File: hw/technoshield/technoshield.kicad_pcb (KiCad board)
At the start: 2 copper layers, 68.6 x 53.3 mm, 9 parts, among them P1 Power, P2 Analog, P3 Digital, P4 Digital, P5 CONN_1, P6 CONN_1, P7 CONN_1, P8 CONN_1

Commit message: During dev PCB.
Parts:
- removed DS2: LCD16X2, Displays:WC1602A
- removed P6, P7, P8: CONN_1, Socket_Arduino_Uno:Arduino_1pin
- added C1: 0.1uF, Capacitors_THT:C_Disc_D3.0mm_W1.6mm_P2.50mm, F.Cu at (128.8, 107.6)
- added C2: 0.1uF, Capacitors_THT:C_Disc_D3.0mm_W1.6mm_P2.50mm, F.Cu at (118.6, 108.0)
- added C3: 0.1uF, Capacitors_THT:C_Disc_D3.0mm_W1.6mm_P2.50mm, F.Cu at (162.8, 84.6)
- added C4: 0.1uF, Capacitors_THT:C_Disc_D3.0mm_W1.6mm_P2.50mm, F.Cu at (149.7, 87.1)
- added C5: 0.1uF, Capacitors_THT:C_Disc_D3.0mm_W1.6mm_P2.50mm, F.Cu at (157.2, 34.2)
- added C6: 0.1uF, Capacitors_THT:C_Disc_D3.0mm_W1.6mm_P2.50mm, F.Cu at (131.8, 125.5)
- added D1: LS T67K-J1K2-1-Z, T67K:T67K, F.Cu at (181.4, 73.5)
- added D2: LY T67K-J2L1-26-Z, T67K:T67K, F.Cu at (185.7, 73.5)
- added D3: LP T67K-E1F2-25-Z, T67K:T67K, F.Cu at (190.0, 73.5)
- added D4: LP T67K-E1F2-25-Z, T67K:T67K, F.Cu at (112.8, 107.4)
- added DS1: LCD-016N002L, Displays:WC1602A, F.Cu at (121.7, 38.0)
- added J1: 101-00303-68-1-ND, Connectors_lib:MICRO_SD_HINGE_AMP, F.Cu at (124.5, 117.0)
- added JP1: JUMPER, Pin_Headers:Pin_Header_Straight_1x02_Pitch2.54mm, F.Cu at (188.1, 130.6)
- added JP2: JUMPER, Pin_Headers:Pin_Header_Straight_1x02_Pitch2.54mm, F.Cu at (181.0, 130.6)
- added JP3: JUMPER, Pin_Headers:Pin_Header_Straight_1x02_Pitch2.54mm, F.Cu at (191.4, 130.6)
- added JP4: JUMPER, Pin_Headers:Pin_Header_Straight_1x02_Pitch2.54mm, F.Cu at (184.3, 130.6)
- added JP5: JUMPER, Pin_Headers:Pin_Header_Straight_1x02_Pitch2.54mm, F.Cu at (173.7, 130.6)
- added JP6: JUMPER, Pin_Headers:Pin_Header_Straight_1x02_Pitch2.54mm, F.Cu at (177.0, 130.6)
- added Q1: MMBT2222A-7-F, TO_SOT_Packages_SMD:SOT-23, F.Cu at (114.0, 86.7)
- added R1: 10k, Resistors_THT:R_Axial_DIN0204_L3.6mm_D1.6mm_P7.62mm_Horizontal, F.Cu at (142.7, 100.2)
- added R11: 1.6k, Resistors_THT:R_Axial_DIN0204_L3.6mm_D1.6mm_P7.62mm_Horizontal, F.Cu at (176.5, 92.1)
- added R12: 1.6k, Resistors_THT:R_Axial_DIN0204_L3.6mm_D1.6mm_P7.62mm_Horizontal, F.Cu at (176.5, 94.5)
- added R13: 1.6k, Resistors_THT:R_Axial_DIN0204_L3.6mm_D1.6mm_P7.62mm_Horizontal, F.Cu at (176.5, 96.9)
- added R14: 4k7, Resistors_THT:R_Axial_DIN0204_L3.6mm_D1.6mm_P7.62mm_Horizontal, F.Cu at (168.9, 101.7)
- added R15: 4k7, Resistors_THT:R_Axial_DIN0204_L3.6mm_D1.6mm_P7.62mm_Horizontal, F.Cu at (168.9, 99.3)
- added R16: 750, Resistors_THT:R_Axial_DIN0204_L3.6mm_D1.6mm_P7.62mm_Horizontal, F.Cu at (115.3, 100.1)
- added R2: 10k, Resistors_THT:R_Axial_DIN0204_L3.6mm_D1.6mm_P7.62mm_Horizontal, F.Cu at (138.2, 100.2)
- added R3: 10k, Resistors_THT:R_Axial_DIN0204_L3.6mm_D1.6mm_P7.62mm_Horizontal, F.Cu at (145.0, 100.2)
- added R4: 10k, Resistors_THT:R_Axial_DIN0204_L3.6mm_D1.6mm_P7.62mm_Horizontal, F.Cu at (140.5, 100.2)
- added R7: 10k, Resistors_THT:R_Axial_DIN0204_L3.6mm_D1.6mm_P7.62mm_Horizontal, F.Cu at (112.9, 92.5)
- added REF***: OSHW-Symbol_13.4x12mm_SilkScreen, Symbols:OSHW-Symbol_13.4x12mm_SilkScreen, B.Cu at (152.1, 54.2)
- added RV1: 10k, POTENTIOMETRES:POTENTIOMETRE_BOURNS_3319P, F.Cu at (123.1, 77.2)
- added SW1: SW_PUSH, smt_btn:smt_btn, F.Cu at (183.6, 85.2)
- added SW2: SW_PUSH, smt_btn:smt_btn, F.Cu at (185.9, 98.7)
- added SW3: SW_PUSH, smt_btn:smt_btn, F.Cu at (194.6, 98.7)
- added SW4: SW_PUSH, smt_btn:smt_btn, F.Cu at (183.6, 107.1)
- added SW5: SW_PUSH, smt_btn:smt_btn, F.Cu at (183.6, 117.2)
- added SW6: SW_PUSH, smt_btn:smt_btn, F.Cu at (155.7, 131.4)
- added U1: PDM1-S5-D15-S, PDM1-S:PDM1-S, F.Cu at (124.5, 131.8)
- added U2: MCP23008, Housings_DIP:DIP-18_W7.62mm_LongPads, F.Cu at (155.1, 87.5)
- added U3: MCP23008, Housings_DIP:DIP-18_W7.62mm_LongPads, F.Cu at (128.8, 104.6)
- added U4: HEF4050B, SO16-3_9mm:SO16-3_9mm, F.Cu at (138.4, 93.9)
- P1: value Power -> CONN_01X03; footprint Socket_Arduino_Uno:Socket_Strip_Arduino_1x08 -> Pin_Headers:Pin_Header_Straight_1x03_Pitch2.54mm
- P2: value Analog -> Power; footprint Socket_Arduino_Uno:Socket_Strip_Arduino_1x06 -> Socket_Arduino_Uno:Socket_Strip_Arduino_1x08
- P3: value Digital -> Analog; footprint Socket_Arduino_Uno:Socket_Strip_Arduino_1x10 -> Socket_Arduino_Uno:Socket_Strip_Arduino_1x06
- P4: footprint Socket_Arduino_Uno:Socket_Strip_Arduino_1x08 -> Socket_Arduino_Uno:Socket_Strip_Arduino_1x10
- P5: value CONN_1 -> Digital; footprint Socket_Arduino_Uno:Arduino_1pin -> Socket_Arduino_Uno:Socket_Strip_Arduino_1x08
- moved P3 57.9 mm to (161.8, 123.8)
- moved P5 57.8 mm to (156.7, 75.6)
- moved P4 26.9 mm to (129.8, 75.6)
- moved P2 22.9 mm to (138.9, 123.8)
- moved P1 8.52 mm to (141.5, 132.0), turned to 90 degrees
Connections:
- P1 pad 2: /IOREF -> Net-(P1-Pad2)
- P1 pad 3: /Reset -> Net-(P1-Pad3)
- P2 pad 1: /A0 -> Net-(P2-Pad1)
- P2 pad 2: /A1 -> /IOREF
- P2 pad 3: /A2 -> /Reset
- P2 pad 4: /A3 -> +3V3
- P2 pad 5: /A4(SDA) -> +5V
- P2 pad 6: /A5(SCL) -> GND
- P3 pad 1: /A5(SCL) -> /A0
- P3 pad 2: /A4(SDA) -> /A1
- P3 pad 3: /AREF -> /A2
- P3 pad 4: GND -> /A3
- P3 pad 5: /13(SCK) -> /A4(SDA)
- P3 pad 6: /12(MISO) -> /A5(SCL)
- P4 pad 1: /7 -> /A5(SCL)
- P4 pad 2: /6(**) -> /A4(SDA)
- P4 pad 3: /5(**) -> /AREF
- P4 pad 4: /4 -> GND
- P4 pad 5: /3(**) -> /13(SCK)
- P4 pad 6: /2 -> /12(MISO)
- P4 pad 7: /1(Tx) -> /11(**/MOSI)
- P4 pad 8: /0(Rx) -> /10(**/SS)
- P5 pad 1: Net-(P5-Pad1) -> /7
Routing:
- net /A5(SCL): track 0.00 -> 177.1 mm, vias 0 -> 2
- net /A4(SDA): track 0.00 -> 130.1 mm
- net +3V3: track 0.00 -> 96.3 mm
- net Net-(DS1-Pad14): track 0.00 -> 76.7 mm
- net Net-(DS1-Pad13): track 0.00 -> 74.4 mm
- net Net-(DS1-Pad11): track 0.00 -> 72.7 mm, vias 0 -> 1
- net Net-(DS1-Pad12): track 0.00 -> 71.0 mm
- net Net-(DS1-Pad6): track 0.00 -> 60.9 mm, vias 0 -> 1
- net Net-(D4-Pad1): track 0.00 -> 57.5 mm, vias 0 -> 2
- net Net-(J1-Pad3): track 0.00 -> 55.4 mm, vias 0 -> 2
- net Net-(DS1-Pad4): track 0.00 -> 53.9 mm
- net Net-(J1-Pad5): track 0.00 -> 53.4 mm, vias 0 -> 4
- net Net-(SW3-Pad1): track 0.00 -> 47.0 mm, vias 0 -> 2
- net Net-(R16-Pad2): track 0.00 -> 44.5 mm, vias 0 -> 1
- net Net-(DS1-Pad3): track 0.00 -> 40.8 mm
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- added copper zone on F.Cu, net +5V
- added copper zone on B.Cu, net GND
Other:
- board size 68.6 x 53.3 mm -> 85.9 x 102.1 mm
- board text added: "+"
- board text added: "-"
- board text added: "0"
- board text added: "12"
- board text added: "13"
- board text added: "2"
- board text added: "3.3V"
- board text added: "4"
- board text added: "5V"
- board text added: "7"
- board text added: "8"
- board text added: "A0"
- board text added: "A1"
- board text added: "A2"
- board text added: "A3"
- board text added: "A4"
- board text added: "A5"
- board text added: "AREF"
- board text added: "But/LED"
- board text added: "GND"
- board text added: "I2C Addr"
- board text added: "I2C Pull-up"
- board text added: "IOREF"
- board text added: "LCD"
- board text added: "PWR +/-15V"
- board text added: "RESET"
- board text added: "RX<-0"
- board text added: "Reset"
- board text added: "SCL"
- board text added: "SDA"
- board text added: "TX->1"
- board text added: "Technoshield - User Interface Dépertement de Génie Physique Cégep La Poactière"
- board text added: "VIN"
- board text added: "_________________"
- board text added: "| Board | Rev: --"
- board text added: "| Technoshield - User Interface | Génie Physique, Cégep La Pocatière"
- board text added: "| |"
- board text added: "~~10"
- board text added: "~~11"
- board text added: "~~3"
- board text added: "~~5"
- board text added: "~~6"
- board text added: "~~9"
- board text removed: "1"

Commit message: Dev of Rev -- almost finish.
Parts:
- moved P1 2.54 mm to (144.0, 132.0), turned to 270 degrees
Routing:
- net Net-(DS1-Pad16): track 0.00 -> 71.1 mm, vias 0 -> 1
- net GND: track 0.00 -> 64.2 mm, vias 0 -> 24
- net Net-(JP4-Pad2): track 16.5 -> 76.6 mm, vias 0 -> 1
- net /12(MISO): track 0.00 -> 59.6 mm, vias 0 -> 2
- net Net-(JP3-Pad2): track 11.2 -> 69.2 mm
- net Net-(JP2-Pad2): track 12.1 -> 69.2 mm
- net Net-(JP1-Pad2): track 14.4 -> 71.3 mm, vias 0 -> 1
- net +5V: track 11.8 -> 55.4 mm, vias 0 -> 2
- net Net-(JP5-Pad1): track 0.00 -> 38.7 mm, vias 0 -> 2
- net /A5(SCL): track 177.1 -> 138.9 mm, vias 2 -> 1
- net Net-(JP6-Pad1): track 0.00 -> 33.4 mm, vias 0 -> 1
- net Net-(D3-Pad2): track 0.00 -> 29.9 mm, vias 0 -> 1
- net Net-(P1-Pad1): track 0.00 -> 27.4 mm
- net Net-(D2-Pad2): track 0.00 -> 23.9 mm, vias 0 -> 1
- net /Reset: track 0.00 -> 23.4 mm
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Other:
- board text added: "Board Rev: --"
- board text added: "Technoshield - User Interface Génie Physique, Cégep La Pocatière"
- board text removed: "| Board | Rev: --"
- board text removed: "| Technoshield - User Interface | Génie Physique, Cégep La Pocatière"

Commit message: Gerber done.
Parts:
- moved C5 38.2 mm to (195.3, 37.2), turned to 270 degrees
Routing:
- net +5V: track 55.4 -> 96.8 mm
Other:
- board size 85.9 x 102.1 mm -> 85.9 x 99.9 mm
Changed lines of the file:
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@@
     (links 126)
     (no_connects 0)
-    (area 104.337905 32.309999 209.860096 138.997)
+    (area 110.922999 34.468999 196.925001 134.568001)
     (thickness 1.6)
-    (drawings 55)
-    (tracks 455)
+    (drawings 56)
+    (tracks 460)
     (zones 0)
     (modules 47)
@@
     (rev --)
     (company "Cégep La Pocatiere")
-    (comment 1 https://creativecommons.org/licenses/by-sa/4.0/)
-    (comment 2 "Released under the Creative Commons Attribution Share-Alike 4.0 License")
-    (comment 3 "Jean-Sébastien Castonguay")
+    (comment 1 "Adapted from https://learn.adafruit.com/i2c-spi-lcd-backpack")
+    (comment 2 https://creativecommons.org/licenses/by-sa/4.0/)
+    (comment 3 "Released under the Creative Commons Attribution Share-Alike 4.0 License")
+    (comment 4 "Copyright 2017 Jean-Sébastien Castonguay")
   )
   (layers
@@
     (pad_drill 1.016)
     (pad_to_mask_clearance 0)
+    (pad_to_paste_clearance -0.127)
     (aux_axis_origin 110.998 126.365)
     (grid_origin 176.53 82.042)
     (visible_elements 7FFFFFFF)
     (pcbplotparams
-      (layerselection 0x00030_80000001)
+      (layerselection 0x010fc_80000001)
       (usegerberextensions false)
       (excludeedgelayer true)
@@
       (drillshape 0)
       (scaleselection 1)
-      (outputdirectory ""))
+      (outputdirectory gerber/))
   )
   (net 0 "")
@@
   )
   (module Capacitors_THT:C_Disc_D3.0mm_W1.6mm_P2.50mm (layer F.Cu)
-    (at 157.226 34.163 180)
+    (at 195.326 37.211 270)
     (descr "C, Disc series, Radial, pin pitch=2.50mm, , diameter*width=3.0*1.6mm^2, Capacitor, http://www.vishay.com/docs/45233/krseries.pdf")
     (tags "C Disc series Radial pin pitch 2.50mm  diameter 3.0mm width 1.6mm Capacitor")
-    (fp_text reference C5 (at 4.699 0.127 180) (layer F.SilkS)
-      (effects (font (size 1 1) (thickness 0.15)))
-    )
-    (fp_text value 0.1uF (at -3.175 0 180) (layer F.SilkS)
+    (fp_text reference C5 (at 4.699 0.127 270) (layer F.SilkS)
+      (effects (font (size 1 1) (thickness 0.15)))
+    )
+    (fp_text value 0.1uF (at 8.128 0.127 270) (layer F.SilkS)
+      (effects (font (size 1 1) (thickness 0.15)))
+    )
+    (fp_line (start -0.25 -0.8) (end -0.25 0.8) (layer F.Fab) (width 0.1))
+    (fp_line (start -0.25 0.8) (end 2.75 0.8) (layer F.Fab) (width 0.1))
+    (fp_line (start 2.75 0.8) (end 2.75 -0.8) (layer F.Fab) (width 0.1))
+    (fp_line (start 2.75 -0.8) (end -0.25 -0.8) (layer F.Fab) (width 0.1))
+    (fp_line (start 0.663 -0.861) (end 1.837 -0.861) (layer F.SilkS) (width 0.12))
+    (fp_line (start 0.663 0.861) (end 1.837 0.861) (layer F.SilkS) (width 0.12))
+    (fp_line (start -1.05 -1.15) (end -1.05 1.15) (layer F.CrtYd) (width 0.05))
+    (fp_line (start -1.05 1.15) (end 3.55 1.15) (layer F.CrtYd) (width 0.05))
+    (fp_line (start 3.55 1.15) (end 3.55 -1.15) (layer F.CrtYd) (width 0.05))
+    (fp_line (start 3.55 -1.15) (end -1.05 -1.15) (layer F.CrtYd) (width 0.05))
+    (pad 1 thru_hole circle (at 0 0 270) (size 1.6 1.6) (drill 0.8) (layers *.Cu *.Mask)
+      (net 3 +5V))
+    (pad 2 thru_hole circle (at 2.5 0 270) (size 1.6 1.6) (drill 0.8) (layers *.Cu *.Mask)
+      (net 4 GND))
+    (model Capacitors_ThroughHole.3dshapes/C_Disc_D3.0mm_W1.6mm_P2.50mm.wrl
+      (at (xyz 0 0 0))
+      (scale (xyz 0.393701 0.393701 0.393701))
+      (rotate (xyz 0 0 0))
+    )
+  )
+  (module Capacitors_THT:C_Disc_D3.0mm_W1.6mm_P2.50mm (layer F.Cu)
+    (at 131.826 125.476 180)
+    (descr "C, Disc series, Radial, pin pitch=2.50mm, , diameter*width=3.0*1.6mm^2, Capacitor, http://www.vishay.com/docs/45233/krseries.pdf")
+    (tags "C Disc series Radial pin pitch 2.50mm  diameter 3.0mm width 1.6mm Capacitor")
+    (fp_text reference C6 (at -2.159 0.127 180) (layer F.SilkS)
+      (effects (font (size 1 1) (thickness 0.15)))
+    )
+    (fp_text value 0.1uF (at 1.25 1.86 180) (layer F.SilkS)
       (effects (font (size 1 1) (thickness 0.15)))
     )
@@
     )
   )
-  (module Capacitors_THT:C_Disc_D3.0mm_W1.6mm_P2.50mm (layer F.Cu)
-    (at 131.826 125.476 180)
-    (descr "C, Disc series, Radial, pin pitch=2.50mm, , diameter*width=3.0*1.6mm^2, Capacitor, http://www.vishay.com/docs/45233/krseries.pdf")
-    (tags "C Disc series Radial pin pitch 2.50mm  diameter 3.0mm width 1.6mm Capacitor")
-    (fp_text reference C6 (at -2.159 0.127 180) (layer F.SilkS)
-      (effects (font (size 1 1) (thickness 0.15)))
-    )
-    (fp_text value 0.1uF (at 1.25 1.86 180) (layer F.SilkS)
-      (effects (font (size 1 1) (thickness 0.15)))
-    )
-    (fp_line (start -0.25 -0.8) (end -0.25 0.8) (layer F.Fab) (width 0.1))
-    (fp_line (start -0.25 0.8) (end 2.75 0.8) (layer F.Fab) (width 0.1))
-    (fp_line (start 2.75 0.8) (end 2.75 -0.8) (layer F.Fab) (width 0.1))
-    (fp_line (start 2.75 -0.8) (end -0.25 -0.8) (layer F.Fab) (width 0.1))
-    (fp_line (start 0.663 -0.861) (end 1.837 -0.861) (layer F.SilkS) (width 0.12))
-    (fp_line (start 0.663 0.861) (end 1.837 0.861) (layer F.SilkS) (width 0.12))
-    (fp_line (start -1.05 -1.15) (end -1.05 1.15) (layer F.CrtYd) (width 0.05))
-    (fp_line (start -1.05 1.15) (end 3.55 1.15) (layer F.CrtYd) (width 0.05))
-    (fp_line (start 3.55 1.15) (end 3.55 -1.15) (layer F.CrtYd) (width 0.05))
-    (fp_line (start 3.55 -1.15) (end -1.05 -1.15) (layer F.CrtYd) (width 0.05))
-    (pad 1 thru_hole circle (at 0 0 180) (size 1.6 1.6) (drill 0.8) (layers *.Cu *.Mask)
-      (net 3 +5V))
-    (pad 2 thru_hole circle (at 2.5 0 180) (size 1.6 1.6) (drill 0.8) (layers *.Cu *.Mask)
-      (net 4 GND))
-    (model Capacitors_ThroughHole.3dshapes/C_Disc_D3.0mm_W1.6mm_P2.50mm.wrl
-      (at (xyz 0 0 0))
-      (scale (xyz 0.393701 0.393701 0.393701))
-      (rotate (xyz 0 0 0))
-    )
-  )
   (module T67K:T67K (layer F.Cu)
     (at 181.356 73.533)
@@
     (descr http://www.kamami.pl/dl/wc1602a0.pdf)
     (tags "LCD 16x2 Alphanumeric 16pin")
-    (fp_text reference DS1 (at -2.99974 -3.59918) (layer F.SilkS)
+    (fp_text reference DS1 (at -9.398 -1.524) (layer F.SilkS)
       (effects (font (size 1 1) (thickness 0.15)))
     )
@@
     )
   )
+  (gr_line (start 196.85 34.544) (end 196.85 134.493) (angle 90) (layer Edge.Cuts) (width 0.15))
+  (gr_line (start 110.998 34.544) (end 111.76 34.544) (angle 90) (layer Edge.Cuts) (width 0.15))
+  (gr_line (start 110.998 134.493) (end 110.998 34.544) (angle 90) (layer Edge.Cuts) (width 0.15))
+  (gr_line (start 110.998 34.544) (end 196.85 34.544) (angle 90) (layer Edge.Cuts) (width 0.15))
   (gr_text "Technoshield - User Interface\nDépertement de Génie Physique\nCégep La Poactière" (at 170.434 64.897) (layer B.SilkS)
     (effects (font (size 1.5 1.5) (thickness 0.3)) (justify left mirror))
   )
-  (gr_line (start 196.85 32.385) (end 110.998 32.385) (angle 90) (layer Edge.Cuts) (width 0.15))
-  (gr_line (start 196.85 134.493) (end 196.85 32.385) (angle 90) (layer Edge.Cuts) (width 0.15))
   (gr_line (start 110.998 134.493) (end 196.85 134.493) (angle 90) (layer Edge.Cuts) (width 0.15))
-  (gr_line (start 110.998 32.385) (end 110.998 134.493) (angle 90) (layer Edge.Cuts) (width 0.15))
   (gr_text "Board\nRev: --" (at 168.402 107.061) (layer F.SilkS)
     (effects (font (size 1.5 1.5) (thickness 0.3) italic) (justify left))
@@
   (segment (start 144.018 126.365) (end 144.018 123.825) (width 0.25) (layer F.Cu) (net 2))
   (segment (start 144.78 127.127) (end 144.018 126.365) (width 0.25) (layer F.Cu) (net 2))
+  (segment (start 195.326 37.211) (end 194.818 37.211) (width 0.25) (layer F.Cu) (net 3))
+  (segment (start 194.818 37.211) (end 192.532 34.925) (width 0.25) (layer F.Cu) (net 3))
+  (segment (start 192.532 34.925) (end 158.369 34.925) (width 0.25) (layer F.Cu) (net 3))
+  (segment (start 158.369 34.925) (end 157.226 36.068) (width 0.25) (layer F.Cu) (net 3))
+  (segment (start 157.226 36.068) (end 157.226 37.973) (width 0.25) (layer F.Cu) (net 3))
   (segment (start 128.778 107.569) (end 128.778 114.173) (width 0.25) (layer B.Cu) (net 3))
   (segment (start 131.826 117.221) (end 131.826 125.476) (width 0.25) (layer F.Cu) (net 3))
@@
     (polygon
       (pts
-        (xy 195.834 133.477) (xy 112.014 133.477) (xy 112.014 33.401) (xy 195.834 33.401)
+        (xy 196.596 134.239) (xy 111.252 134.239) (xy 111.252 34.798) (xy 196.596 34.798)
       )
     )
@@
     (polygon
       (pts
-        (xy 195.834 133.477) (xy 112.014 133.477) (xy 112.014 33.401) (xy 195.834 33.401)
+        (xy 196.596 134.239) (xy 111.252 134.239) (xy 111.252 34.798) (xy 196.596 34.798)
       )
     )

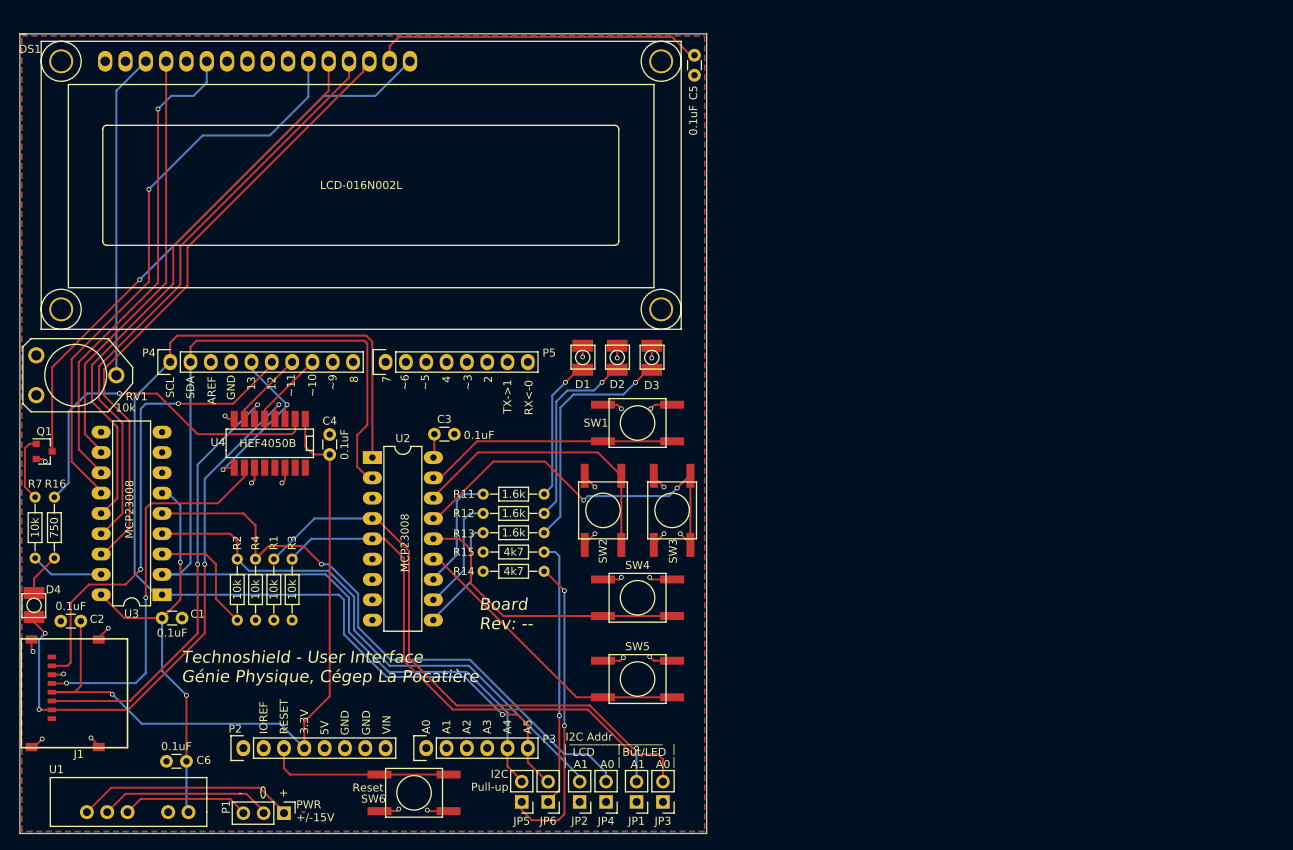
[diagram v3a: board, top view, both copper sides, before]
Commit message: Issue #1: Problems found in prototype rev-- Problem with USB and component contact fixed.
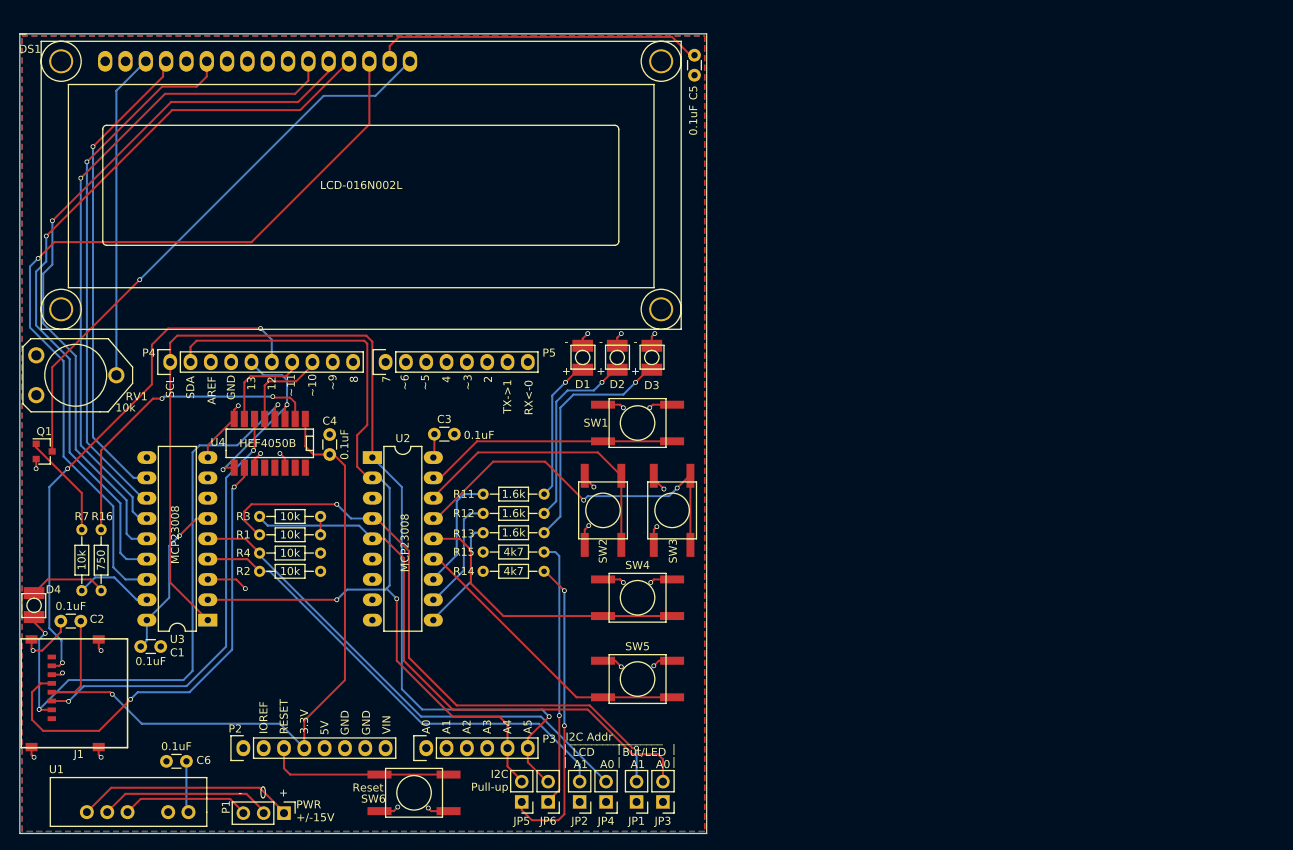
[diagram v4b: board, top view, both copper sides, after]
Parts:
- moved R16 7.12 mm to (121.2, 104.1)
- moved R7 7.12 mm to (118.7, 96.5)
- moved R3 6.71 mm to (141.0, 94.9), turned to 0 degrees
- moved U3 6.54 mm to (134.5, 107.8)
- moved C1 4.44 mm to (126.1, 111.1)
- moved R1 3.53 mm to (141.0, 97.2), turned to 0 degrees
- moved R2 3.18 mm to (141.0, 101.7), turned to 0 degrees
- moved R4 0.92 mm to (141.0, 99.4), turned to 0 degrees
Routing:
- net Net-(DS1-Pad14): track 78.3 -> 105.5 mm, vias 0 -> 1
- net +5V: track 96.8 -> 71.1 mm, vias 2 -> 1
- net Net-(DS1-Pad13): track 74.4 -> 95.0 mm, vias 0 -> 1
- net Net-(DS1-Pad12): track 71.0 -> 90.3 mm, vias 0 -> 1
- net /A4(SDA): track 135.0 -> 116.4 mm, vias 0 -> 2
- net Net-(JP4-Pad2): track 76.6 -> 62.8 mm, vias 1 -> 0
- net Net-(J1-Pad5): track 48.0 -> 59.5 mm
- net Net-(DS1-Pad11): track 72.7 -> 82.4 mm
- net Net-(JP2-Pad2): track 69.2 -> 59.9 mm
- net /12(MISO): track 59.6 -> 66.8 mm, vias 2 -> 3
- net GND: track 64.2 -> 71.1 mm, vias 24 -> 25
- net Net-(JP1-Pad2): track 71.3 -> 77.8 mm, vias 1 -> 2
- net Net-(D4-Pad1): track 71.5 -> 77.6 mm, vias 4 -> 3
- net Net-(DS1-Pad6): track 60.9 -> 66.7 mm
- net Net-(DS1-Pad4): track 53.9 -> 59.6 mm, vias 0 -> 1
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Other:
- board text added: "Booard rev: A"
- board text removed: "Board Rev: --"
- board text removed: "Technoshield - User Interface Génie Physique, Cégep La Pocatière"

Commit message: Add logo.
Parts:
- added G***: LOGO, logo:logo, B.Cu at (185.4, 59.4)
- added G***: LOGO, logo:logo, F.Cu at (144.7, 110.4)
- moved REF*** 32.6 mm to (120.4, 46.7)
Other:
- board text added: "Technoshield - User Interface Board Rev: A Département de technologie du génie physique Cégep La Pocatière"
- board text added: "Technoshield User Interface"
- board text added: "open source hardware"
- board text removed: "Booard rev: A"
- board text removed: "Technoshield - User Interface Dépertement de Génie Physique Cégep La Poactière"
